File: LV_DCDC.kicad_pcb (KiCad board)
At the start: 4 copper layers, 160 x 70 mm, 115 parts, among them J101 1017503, J102 1017503, J201 5023860270, J202 Conn_01x05, J203 Conn_01x04, J204 Conn_01x04, U201 STM32G431KBT6, U301 TCAN1462VDRQ1, U302 ESDCAN24-2BLY, U401 LMR50410YFQDBVRQ1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

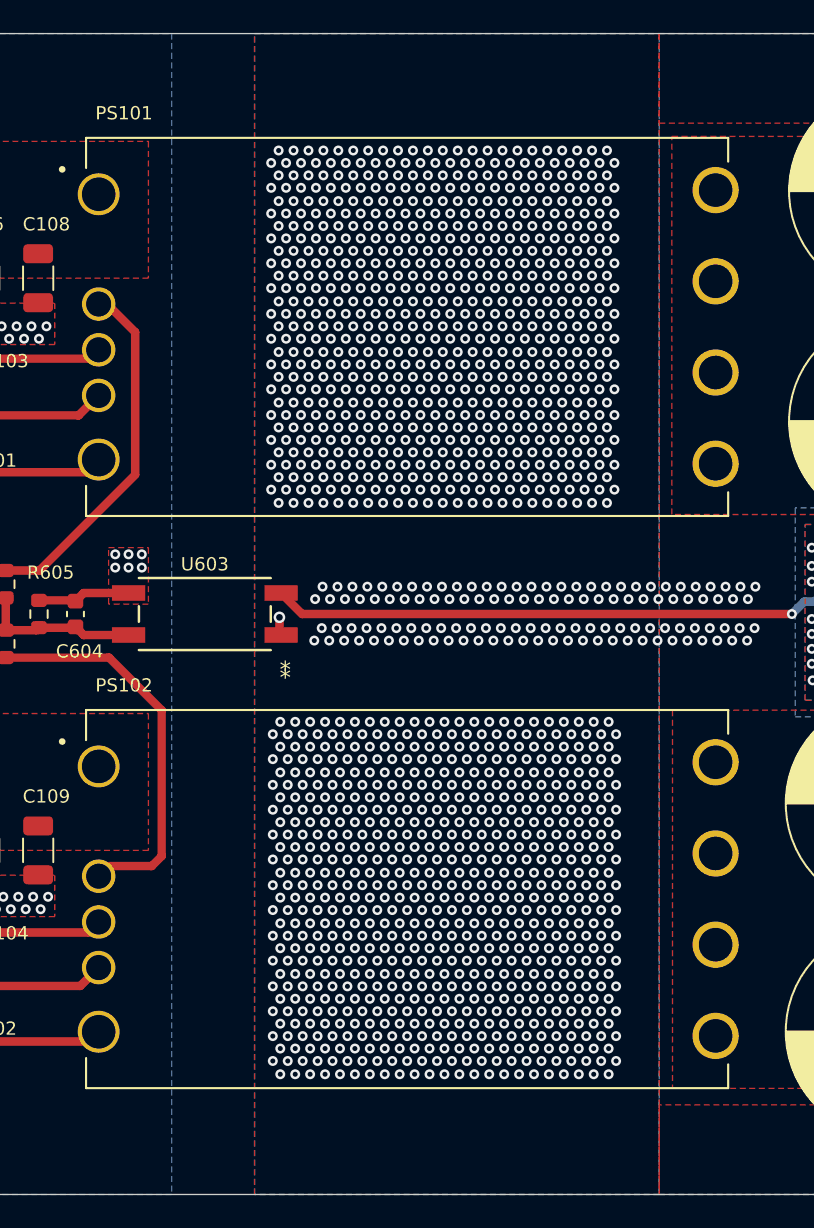
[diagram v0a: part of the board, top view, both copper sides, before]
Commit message: heat sink mount holes
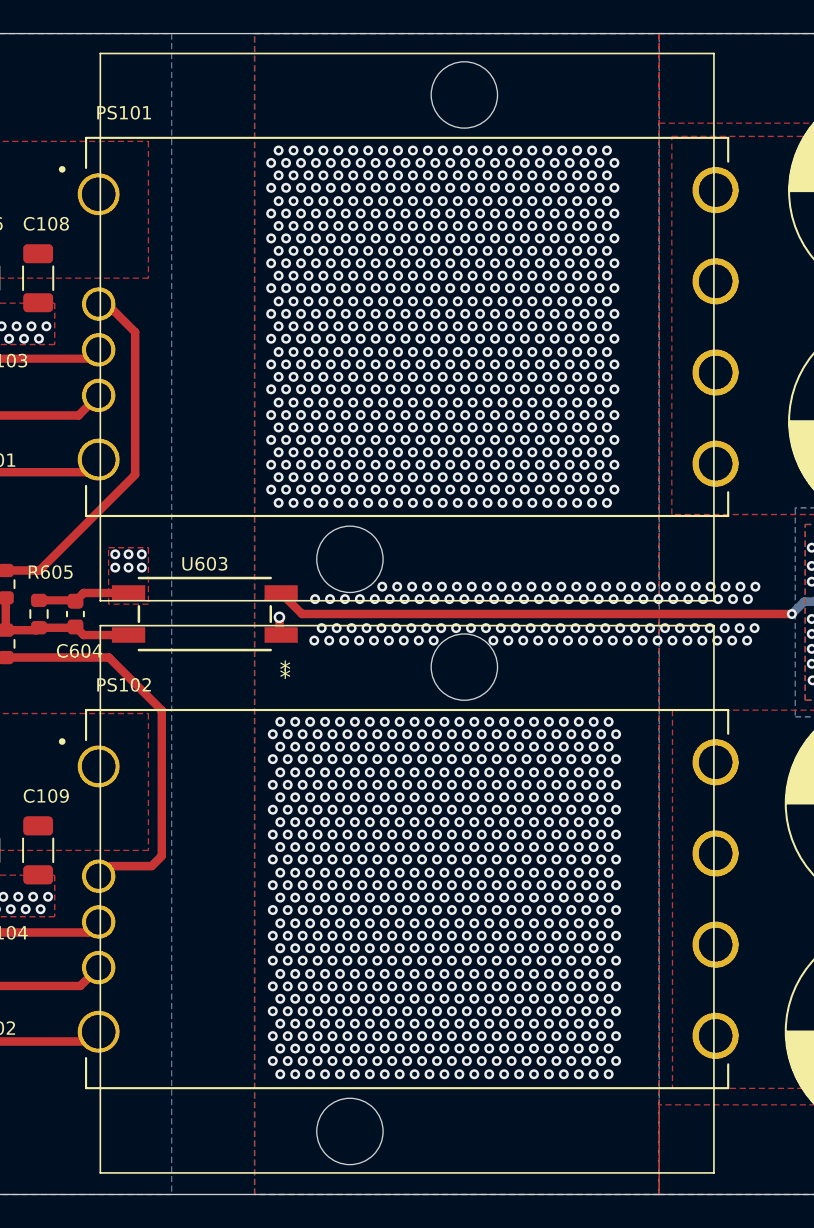
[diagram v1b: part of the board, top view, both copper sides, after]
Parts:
- added REF**: libra, Library:libra, F.Cu at (108.0, 92.2)
- added REF**: libra, Library:libra, F.Cu at (108.0, 57.7)
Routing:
- net GND: vias 1494 -> 1487
